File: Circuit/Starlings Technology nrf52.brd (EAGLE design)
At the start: 53.3 x 52.7 mm, 58 parts, among them J4 USB Micro, J7 CORTEX_DEBUG_SMD, Q2 BSS84, SW1 FSM8JSMASTR, SW2 FSM8JSMASTR, U2 MCP73831, U3 BC840M, U4 MIC5317 (MIC5205), U5 74AHCT2G125, U8 TPS61235P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

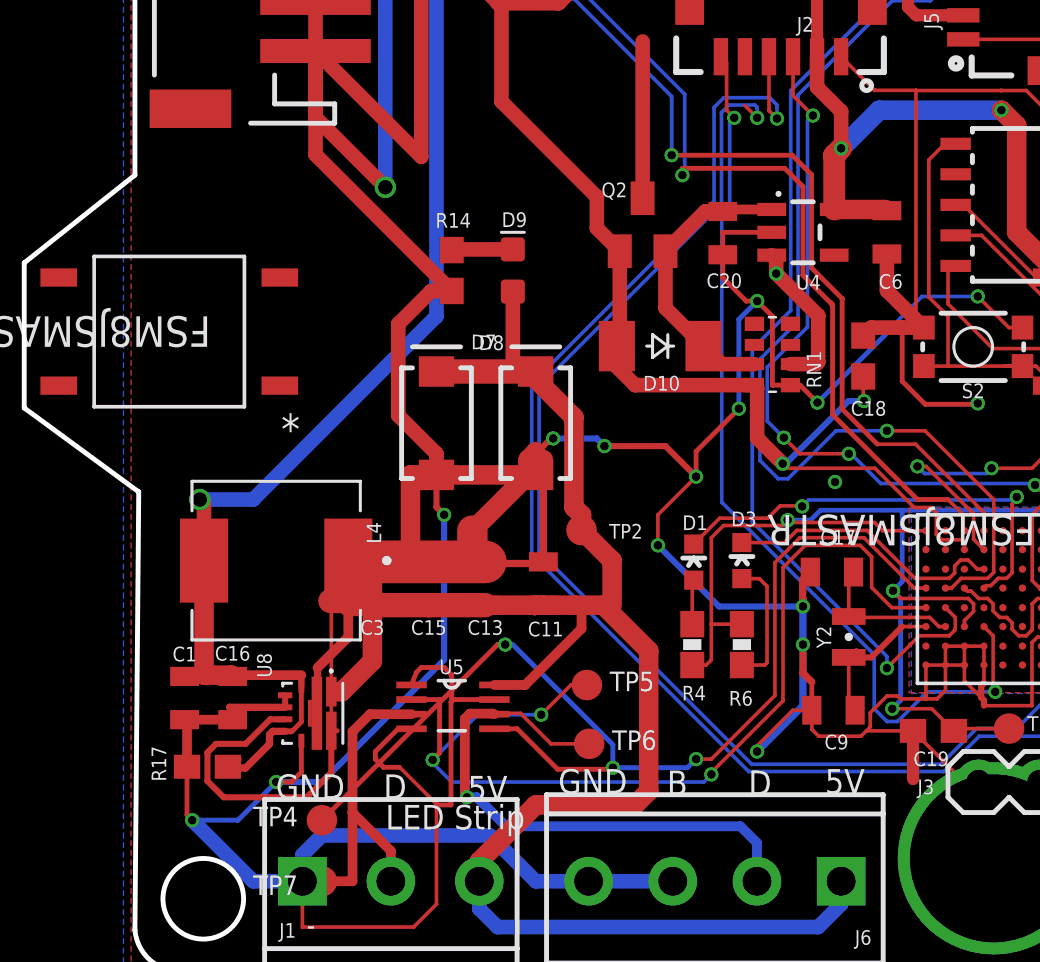
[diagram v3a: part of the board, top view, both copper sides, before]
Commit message: Revision 10
- Adding second tactile switch
- Adjusting board dimensions to place buttons
- Adding rocker on/off switch
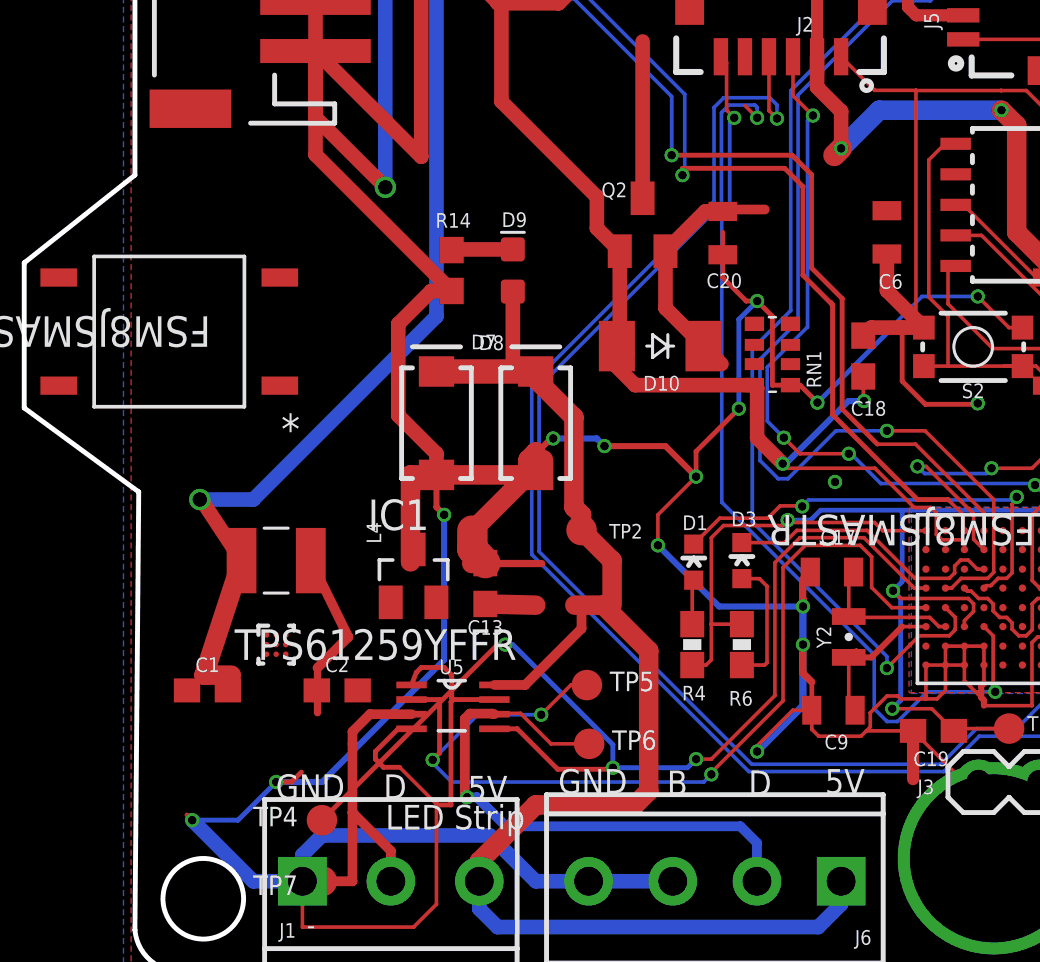
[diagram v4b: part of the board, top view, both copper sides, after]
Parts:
- removed C11, C15, C16, C3: 22uF, SparkFun-Capacitors:0805
- removed R17: 1M, SparkFun-Resistors:0603@1
- removed U4: MIC5317 (MIC5205), SparkFun-IC-Power:SOT23-5
- removed U8: TPS61235P, TPS61235PRWLR:CONV_TPS61235PRWLR
- added C2: 10uF, SparkFun-Capacitors:0603
- added IC1: MCP1703CB, linear:SOT23
- added U1: TPS61259YFFR, TPS6125x:YFF0009ACAG
- C1, C13: value 22uF -> 10uF; device SparkFun-Capacitors:0805 -> SparkFun-Capacitors:0603
- L4: device FDSD0630-H-1R0M_P3:IND_FDSD0630-H-1R0M=P3 -> 1277AS-H-1R0M_P2:INDC3225X120N
- moved C1 1.00 mm to (-0.95, 12.1), turned to 0 degrees
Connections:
- removed net N$5: RN1.2, U4.3
- removed net N$6: U4.4
- net 3.3V: now also IC1.2; no longer U4.5
- net 5V: now also C2.1, U1.A1, U1.A2; no longer C11.1, C15.1, C3.1, U8.6, U8.9
- net GND: now also C2.2, IC1.1, U1.C1, U1.C2, U1.C3; no longer C11.2, C15.2, C16.2, C3.2, R17.1, U4.2, U8.1, U8.4, U8.5, U8.8
- net N$3: now also U1.B1, U1.B2; no longer U8.2
- net N$4: now also IC1.3; no longer RN1.7, U4.1
- net VBAT: now also U1.A3, U1.B3; no longer C16.1, R17.2, U8.3, U8.7
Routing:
- net GND: track 340.7 -> 305.5 mm
- net 5V: track 95.6 -> 67.6 mm
- net VBAT: track 61.3 -> 50.2 mm
- net N$5: track 6.44 -> 0.00 mm, vias 1 -> 0
- net 3.3V: track 93.5 -> 89.1 mm
- net N$4: track 12.3 -> 10.7 mm
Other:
- board text added: "Swarm Lights V10 3/11/2022 starlings.technology"
- board text removed: "[bike]swarm V9 6/24/2021 swarms.city"

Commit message: traces
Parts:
- moved J3 7.30 mm to (23.8, 8.26)
- moved TP8 2.25 mm to (34.4, 9.37)
- moved TP7 1.59 mm to (5.08, 3.17)
- moved S2 0.71 mm to (30.6, 25.7)
- moved J7 0.71 mm to (32.3, 32.9)
- moved C18 0.32 mm to (26.3, 25.7)
- moved SW2 0.32 mm to (38.7, 26.7), turned to 0 degrees
- moved D3 0.25 mm to (21.5, 17.5)
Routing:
- net SWITCH_1: track 18.6 -> 83.0 mm
- net PIN_03: track 55.1 -> 113.8 mm, vias 2 -> 6
- net SWITCH_2: track 0.00 -> 47.6 mm, vias 0 -> 5
- net VBAT: track 50.2 -> 96.0 mm
- net 5V: track 67.6 -> 92.5 mm
- net 3.3V: track 89.1 -> 112.3 mm, vias 6 -> 9
- net PIN_02: track 60.4 -> 81.2 mm, vias 2 -> 7
- net GND: track 305.5 -> 285.1 mm, vias 17 -> 21
- net N$4: track 10.7 -> 29.4 mm, vias 0 -> 2
- net HEADLAMP_3V3: track 45.6 -> 56.5 mm
- net PIN_01: track 33.4 -> 43.0 mm, vias 4 -> 6
- net VBAT_RAW: track 43.9 -> 35.4 mm
- net SWDIO: track 15.7 -> 18.8 mm
- net SDA: track 40.6 -> 43.2 mm
- net N$3: track 7.22 -> 5.29 mm
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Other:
- board text added: "swarms.city"
- board text removed: "[bike]swarm swarms.city"

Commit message: Adjusting traces, submitting to board house.
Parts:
- moved L4 6.98 mm to (1.91, 10.5)
- moved C2 2.01 mm to (3.81, 14.0), turned to 90 degrees
- moved C1 2.01 mm to (-0.32, 14.0), turned to 90 degrees
- moved POWER_IN 1.59 mm to (-0.16, 38.1)
- turned U1 to 180 degrees
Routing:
- net GND: track 285.1 -> 333.3 mm
- net N$3: track 5.29 -> 14.3 mm, vias 0 -> 4
- net 5V: track 92.5 -> 88.8 mm
- net VBAT: track 96.0 -> 99.3 mm
- net VBAT_RAW: track 35.4 -> 37.8 mm
- net SWITCH_1: track 83.0 -> 81.5 mm
- net PIN_02: track 81.2 -> 81.8 mm
